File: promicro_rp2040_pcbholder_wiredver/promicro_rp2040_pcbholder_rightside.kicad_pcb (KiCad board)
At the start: 2 copper layers, 34.3 x 38.4 mm, 7 parts, among them J1 Conn_01x08_Pin, J2 Conn_01x08_Pin, U1 RP2040_Pro_Micro, U2 TRRS

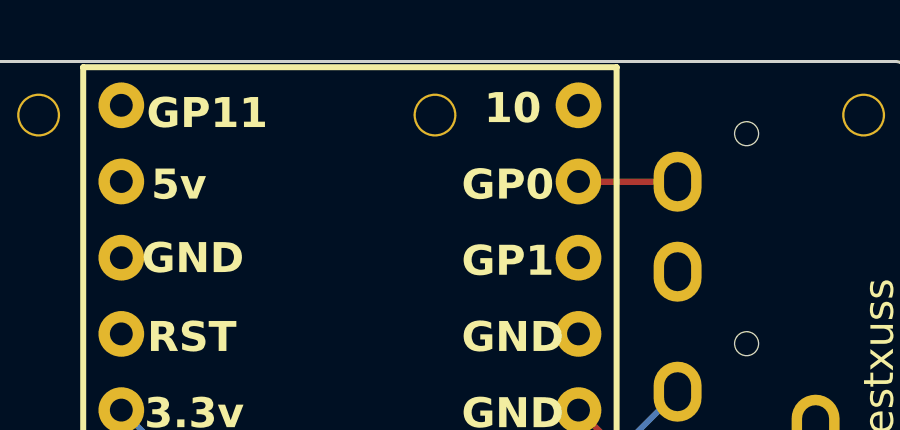
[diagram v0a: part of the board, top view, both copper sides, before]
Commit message: slight change m1.4 right side pcb hole spacing
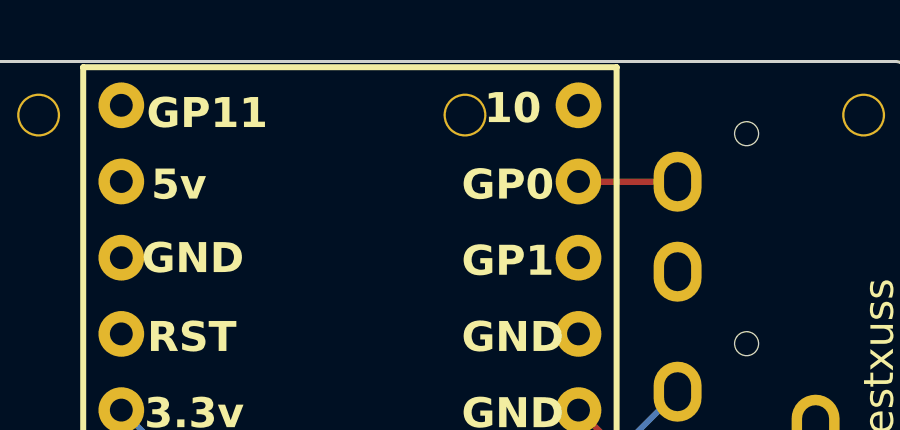
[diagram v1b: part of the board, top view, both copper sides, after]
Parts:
- moved ? 1.00 mm to (150.9, 21.8)
